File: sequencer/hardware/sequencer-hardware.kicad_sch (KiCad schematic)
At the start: 60 parts, among them J1 Barrel Jack, J2 40Pin 0.1", J3 USB_B_Micro, J4 Conn_01x02_Male, J5 JST 4-Pin male, J6 TS Out, SW1 PWR, SW2 SW_Push, U1 L7805_A, U2 L7805_D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

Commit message: Add testpoints
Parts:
- added TP1, TP2, TP3, TP4, TP5, TP6, TP7, TP8: TestPoint, TestPoint:TestPoint_Pad_D1.5mm, symbol Connector:TestPoint
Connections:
- net +3V3: now also TP7.1
- net +5VA: now also TP2.1
- net +5VD: now also TP5.1
- net -5V: now also TP4.1
- net CBUS_NEXTPRSNT: now also TP1.1
- net GNDA: now also TP3.1
- net GNDD: now also TP8.1
- net RUN: now also TP6.1
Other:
- moved on the sheet: C45, C46, C47, C48

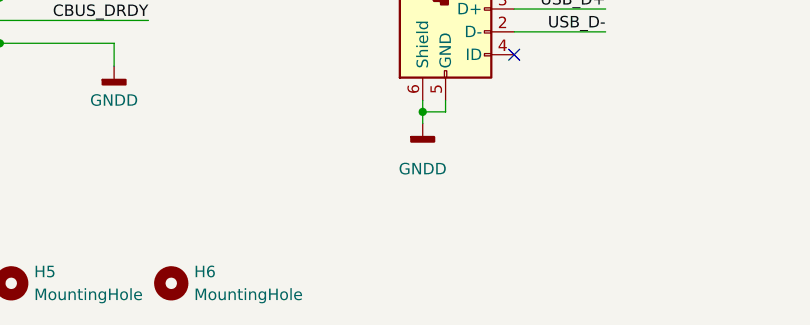
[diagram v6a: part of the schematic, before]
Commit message: Add final mounting hole and generate STEP file
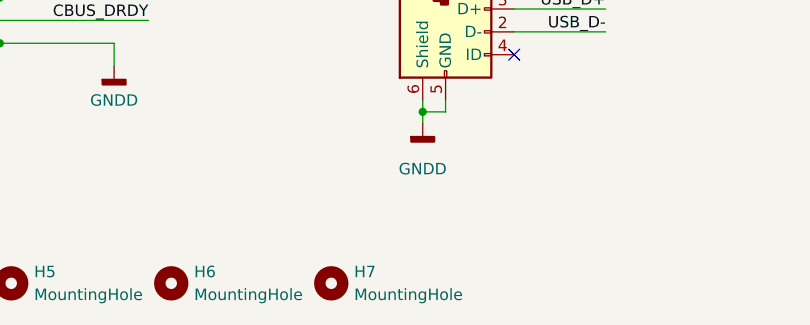
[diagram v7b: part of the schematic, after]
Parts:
- added H7: MountingHole, MountingHole:MountingHole_3.2mm_M3_ISO14580, symbol Mechanical:MountingHole
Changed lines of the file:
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@@
     (pin "1")
+  )
+  (symbol (lib_id "Mechanical:MountingHole") (at 105.41 199.39 0) (unit 1)
+    (in_bom yes) (on_board yes) (fields_autoplaced)
+    (property "Reference" "H7" (id 0) (at 107.95 198.1199 0)
+      (effects (font (size 1.27 1.27)) (justify left))
+    )
+    (property "Value" "MountingHole" (id 1) (at 107.95 200.6599 0)
+      (effects (font (size 1.27 1.27)) (justify left))
+    )
+    (property "Footprint" "MountingHole:MountingHole_3.2mm_M3_ISO14580" (id 2) (at 105.41 199.39 0)
+      (effects (font (size 1.27 1.27)) hide)
+    )
+    (property "Datasheet" "~" (id 3) (at 105.41 199.39 0)
+      (effects (font (size 1.27 1.27)) hide)
+    )
   )
   (symbol (lib_id "Device:C") (at 210.82 124.46 90) (unit 1)
@@
       (reference "H6") (unit 1) (value "MountingHole") (footprint "MountingHole:MountingHole_3.2mm_M3_ISO14580")
     )
+    (path "/add4a986-5a60-4baf-8616-4f7d7cd0fb13"
+      (reference "H7") (unit 1) (value "MountingHole") (footprint "MountingHole:MountingHole_3.2mm_M3_ISO14580")
+    )
     (path "/e7d77e35-7d0f-418c-bddb-e70c65e01157"
